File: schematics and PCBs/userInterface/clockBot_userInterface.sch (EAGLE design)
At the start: 6 parts

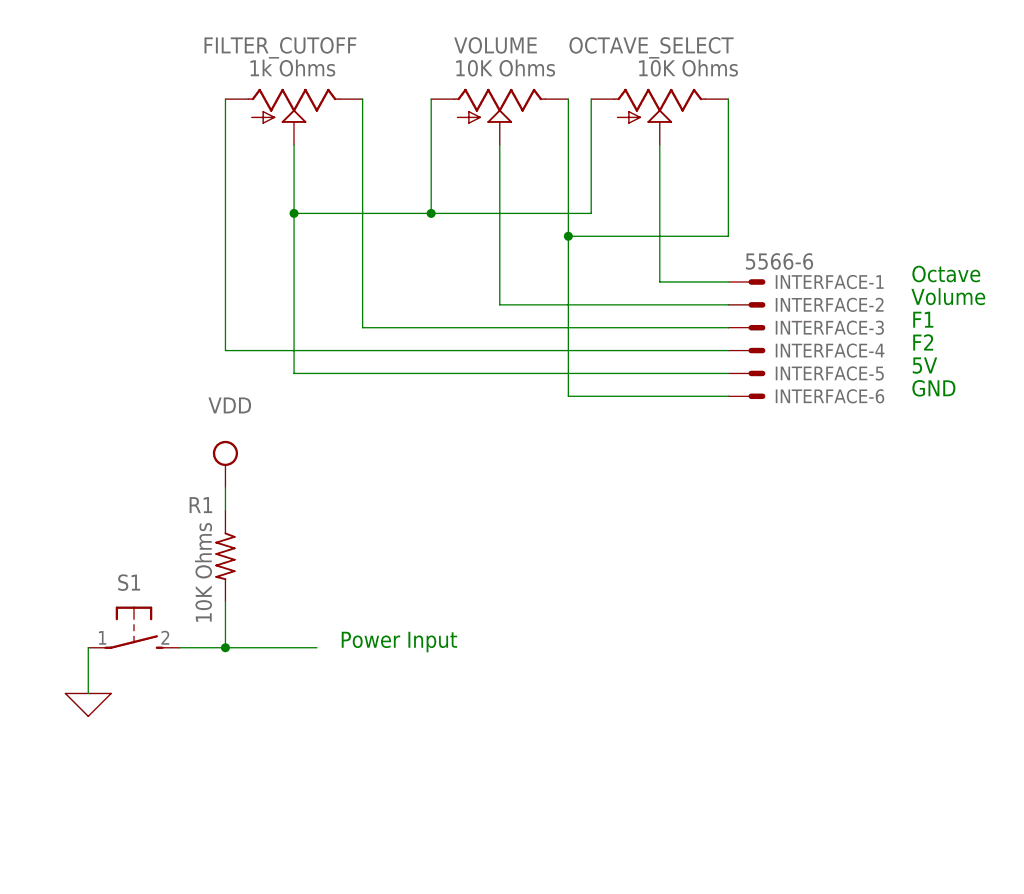
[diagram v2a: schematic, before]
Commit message: Updated user interface
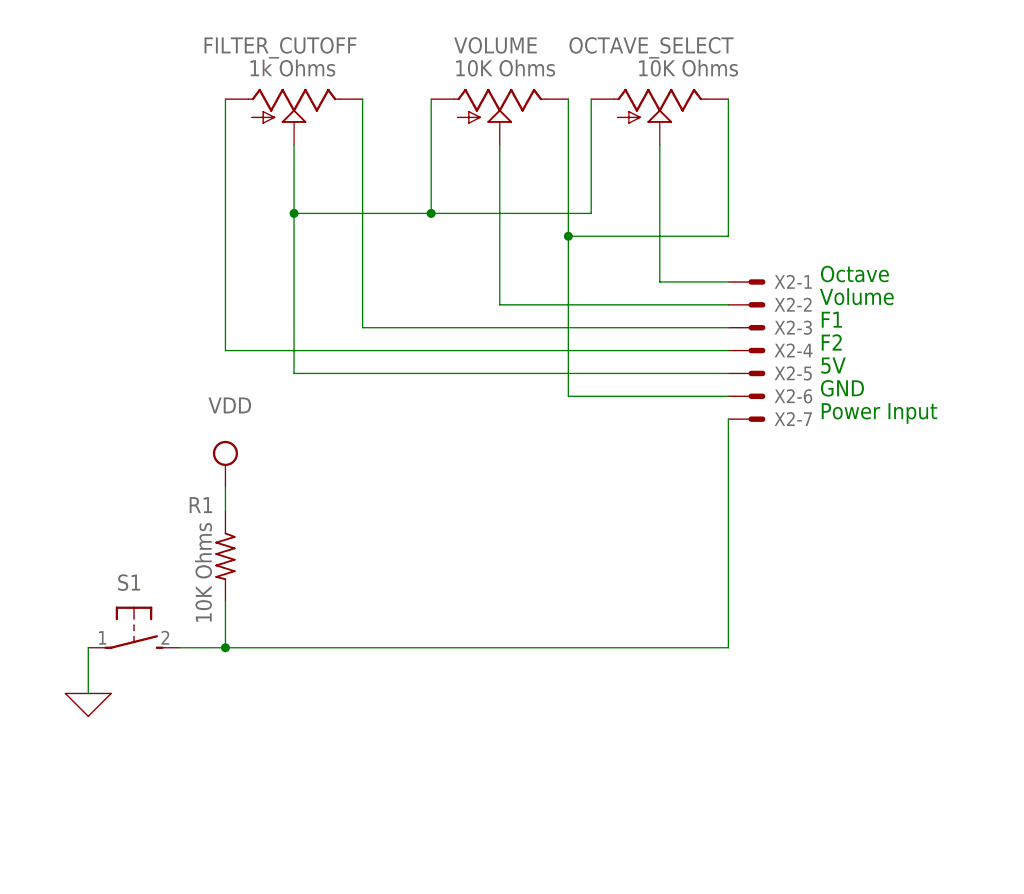
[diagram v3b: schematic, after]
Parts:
- removed INTERFACE: 5566-6, con-molex:5566-6
- added X2: (no value), con-molex:KK-156-7
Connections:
- net N$1: now also X2-7.S
- net N$10: now also X2-2.S; no longer INTERFACE-2.S
- net N$2: now also X2-4.S; no longer INTERFACE-4.S
- net N$3: now also X2-3.S; no longer INTERFACE-3.S
- net N$4: now also X2-5.S; no longer INTERFACE-5.S
- net N$5: now also X2-6.S; no longer INTERFACE-6.S
- net N$8: now also X2-1.S; no longer INTERFACE-1.S
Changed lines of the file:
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@@
 <part name="OCTAVE_SELECT" library="pot" library_urn="urn:adsk.eagle:library:331" deviceset="TRIM_US-" device="S64W" package3d_urn="urn:adsk.eagle:package:22708/1" value="10K Ohms"/>
 <part name="S1" library="adafruit" library_urn="urn:adsk.eagle:library:420" deviceset="31-XX" device="" package3d_urn="urn:adsk.eagle:package:6240698/1"/>
-<part name="INTERFACE" library="con-molex" library_urn="urn:adsk.eagle:library:165" deviceset="5566-6" device="" package3d_urn="urn:adsk.eagle:package:8078581/1"/>
 <part name="SUPPLY1" library="supply2" library_urn="urn:adsk.eagle:library:372" deviceset="VDD" device=""/>
 <part name="X_1" library="ngspice-simulation" library_urn="urn:adsk.eagle:library:527439" deviceset="GND" device=""/>
 <part name="R1" library="adafruit" library_urn="urn:adsk.eagle:library:420" deviceset="FLIPFLOP-RES" device="" package3d_urn="urn:adsk.eagle:package:6240726/1" value="10K Ohms"/>
+<part name="X2" library="con-molex" library_urn="urn:adsk.eagle:library:165" deviceset="KK-156-7" device="" package3d_urn="urn:adsk.eagle:package:8078811/1"/>
 </parts>
 <sheets>
 <sheet>
 <plain>
-<text x="91.44" y="40.64" size="1.778" layer="91">Octave</text>
-<text x="91.44" y="38.1" size="1.778" layer="91">Volume</text>
-<text x="91.44" y="35.56" size="1.778" layer="91">F1</text>
-<text x="91.44" y="33.02" size="1.778" layer="91">F2</text>
-<text x="91.44" y="30.48" size="1.778" layer="91">5V</text>
-<text x="91.44" y="27.94" size="1.778" layer="91">GND</text>
-<text x="27.94" y="0" size="1.778" layer="91">Power Input</text>
+<text x="81.28" y="40.64" size="1.778" layer="91">Octave</text>
+<text x="81.28" y="38.1" size="1.778" layer="91">Volume</text>
+<text x="81.28" y="35.56" size="1.778" layer="91">F1</text>
+<text x="81.28" y="33.02" size="1.778" layer="91">F2</text>
+<text x="81.28" y="30.48" size="1.778" layer="91">5V</text>
+<text x="81.28" y="27.94" size="1.778" layer="91">GND</text>
+<text x="81.28" y="25.4" size="1.778" layer="91">Power Input</text>
 </plain>
 <instances>
@@
 <attribute name="VALUE" x="8.255" y="3.81" size="1.778" layer="96"/>
 </instance>
-<instance part="INTERFACE" gate="-1" x="73.66" y="40.64" smashed="yes">
-<attribute name="NAME" x="76.2" y="39.878" size="1.524" layer="95"/>
-<attribute name="VALUE" x="72.898" y="42.037" size="1.778" layer="96"/>
-</instance>
-<instance part="INTERFACE" gate="-2" x="73.66" y="38.1" smashed="yes">
-<attribute name="NAME" x="76.2" y="37.338" size="1.524" layer="95"/>
-</instance>
-<instance part="INTERFACE" gate="-3" x="73.66" y="35.56" smashed="yes">
-<attribute name="NAME" x="76.2" y="34.798" size="1.524" layer="95"/>
-</instance>
-<instance part="INTERFACE" gate="-4" x="73.66" y="33.02" smashed="yes">
-<attribute name="NAME" x="76.2" y="32.258" size="1.524" layer="95"/>
-</instance>
-<instance part="INTERFACE" gate="-5" x="73.66" y="30.48" smashed="yes">
-<attribute name="NAME" x="76.2" y="29.718" size="1.524" layer="95"/>
-</instance>
-<instance part="INTERFACE" gate="-6" x="73.66" y="27.94" smashed="yes">
-<attribute name="NAME" x="76.2" y="27.178" size="1.524" layer="95"/>
-</instance>
 <instance part="SUPPLY1" gate="G$1" x="15.24" y="20.32" smashed="yes">
 <attribute name="VALUE" x="13.335" y="26.035" size="1.778" layer="96"/>
@@
 <attribute name="NAME" x="13.97" y="16.7386" size="1.778" layer="95" rot="R180"/>
 <attribute name="VALUE" x="11.938" y="13.97" size="1.778" layer="96" rot="R270"/>
+</instance>
+<instance part="X2" gate="-1" x="73.66" y="40.64" smashed="yes">
+<attribute name="NAME" x="76.2" y="39.878" size="1.524" layer="95"/>
+<attribute name="VALUE" x="72.898" y="42.037" size="1.778" layer="96"/>
+</instance>
+<instance part="X2" gate="-2" x="73.66" y="38.1" smashed="yes">
+<attribute name="NAME" x="76.2" y="37.338" size="1.524" layer="95"/>
+</instance>
+<instance part="X2" gate="-3" x="73.66" y="35.56" smashed="yes">
+<attribute name="NAME" x="76.2" y="34.798" size="1.524" layer="95"/>
+</instance>
+<instance part="X2" gate="-4" x="73.66" y="33.02" smashed="yes">
+<attribute name="NAME" x="76.2" y="32.258" size="1.524" layer="95"/>
+</instance>
+<instance part="X2" gate="-5" x="73.66" y="30.48" smashed="yes">
+<attribute name="NAME" x="76.2" y="29.718" size="1.524" layer="95"/>
+</instance>
+<instance part="X2" gate="-6" x="73.66" y="27.94" smashed="yes">
+<attribute name="NAME" x="76.2" y="27.178" size="1.524" layer="95"/>
+</instance>
+<instance part="X2" gate="-7" x="73.66" y="25.4" smashed="yes">
+<attribute name="NAME" x="76.2" y="24.638" size="1.524" layer="95"/>
 </instance>
 </instances>
@@
 <pinref part="FILTER_CUTOFF" gate="G$1" pin="E"/>
 <wire x1="30.48" y1="60.96" x2="30.48" y2="35.56" width="0.1524" layer="91"/>
-<pinref part="INTERFACE" gate="-3" pin="S"/>
 <wire x1="30.48" y1="35.56" x2="71.12" y2="35.56" width="0.1524" layer="91"/>
+<pinref part="X2" gate="-3" pin="S"/>
 </segment>
 </net>
 <net name="N$8" class="0">
 <segment>
-<pinref part="INTERFACE" gate="-1" pin="S"/>
 <wire x1="63.5" y1="40.64" x2="71.12" y2="40.64" width="0.1524" layer="91"/>
 <pinref part="OCTAVE_SELECT" gate="G$1" pin="S"/>
 <wire x1="63.5" y1="55.88" x2="63.5" y2="40.64" width="0.1524" layer="91"/>
+<pinref part="X2" gate="-1" pin="S"/>
 </segment>
 </net>
 <net name="N$10" class="0">
 <segment>
-<pinref part="INTERFACE" gate="-2" pin="S"/>
 <wire x1="45.72" y1="38.1" x2="71.12" y2="38.1" width="0.1524" layer="91"/>
 <pinref part="VOLUME" gate="G$1" pin="S"/>
 <wire x1="45.72" y1="55.88" x2="45.72" y2="38.1" width="0.1524" layer="91"/>
+<pinref part="X2" gate="-2" pin="S"/>
 </segment>
 </net>
@@
 <segment>
 <pinref part="FILTER_CUTOFF" gate="G$1" pin="A"/>
-<pinref part="INTERFACE" gate="-4" pin="S"/>
 <wire x1="15.24" y1="60.96" x2="15.24" y2="33.02" width="0.1524" layer="91"/>
 <wire x1="15.24" y1="33.02" x2="71.12" y2="33.02" width="0.1524" layer="91"/>
+<pinref part="X2" gate="-4" pin="S"/>
 </segment>
 </net>
@@
 <pinref part="FILTER_CUTOFF" gate="G$1" pin="S"/>
 <wire x1="22.86" y1="48.26" x2="22.86" y2="55.88" width="0.1524" layer="91"/>
-<pinref part="INTERFACE" gate="-5" pin="S"/>
 <wire x1="22.86" y1="48.26" x2="22.86" y2="30.48" width="0.1524" layer="91"/>
 <wire x1="22.86" y1="30.48" x2="71.12" y2="30.48" width="0.1524" layer="91"/>
 <junction x="22.86" y="48.26"/>
+<pinref part="X2" gate="-5" pin="S"/>
 </segment>
 </net>
@@
 <pinref part="S1" gate="1" pin="S"/>
 <wire x1="10.16" y1="0" x2="15.24" y2="0" width="0.1524" layer="91"/>
-<wire x1="15.24" y1="0" x2="25.4" y2="0" width="0.1524" layer="91"/>
 <junction x="15.24" y="0"/>
+<pinref part="X2" gate="-7" pin="S"/>
+<wire x1="15.24" y1="0" x2="71.12" y2="0" width="0.1524" layer="91"/>
+<wire x1="71.12" y1="0" x2="71.12" y2="25.4" width="0.1524" layer="91"/>
 </segment>
 </net>
@@
 <wire x1="71.12" y1="60.96" x2="71.12" y2="45.72" width="0.1524" layer="91"/>
 <wire x1="53.34" y1="45.72" x2="71.12" y2="45.72" width="0.1524" layer="91"/>
-<pinref part="INTERFACE" gate="-6" pin="S"/>
 <wire x1="53.34" y1="45.72" x2="53.34" y2="27.94" width="0.1524" layer="91"/>
 <wire x1="53.34" y1="27.94" x2="71.12" y2="27.94" width="0.1524" layer="91"/>
 <junction x="53.34" y="45.72"/>
+<pinref part="X2" gate="-6" pin="S"/>
 </segment>
 </net>
